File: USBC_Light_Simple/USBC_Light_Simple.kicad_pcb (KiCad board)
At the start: 2 copper layers, 79.5 x 40 mm, 11 parts, among them IC1 AP33772SDKZ-13-FA01, J1 USB_C_Receptacle, U1 XHP50B-00-0000-0D0BJ440E, U2 AL8861MP-13, U3 XHP50B-00-0000-0D0BJ440E, U4 XHP50B-00-0000-0D0BJ440E, U5 STM32C011F6Px, U6 AL8861MP-13, U7 XHP50B-00-0000-0D0BJ440E, U8 XHP50B-00-0000-0D0BJ440E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

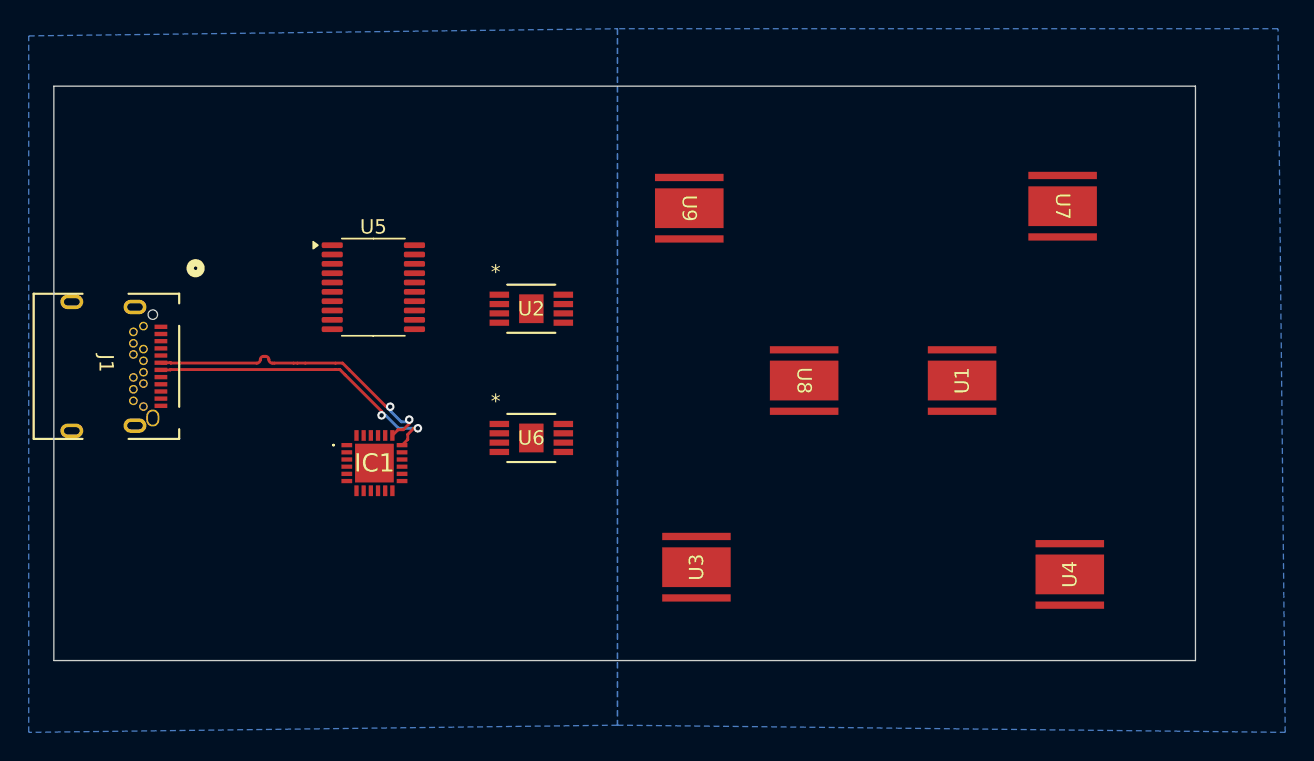
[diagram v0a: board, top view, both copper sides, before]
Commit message: Preliminary component placement on board.
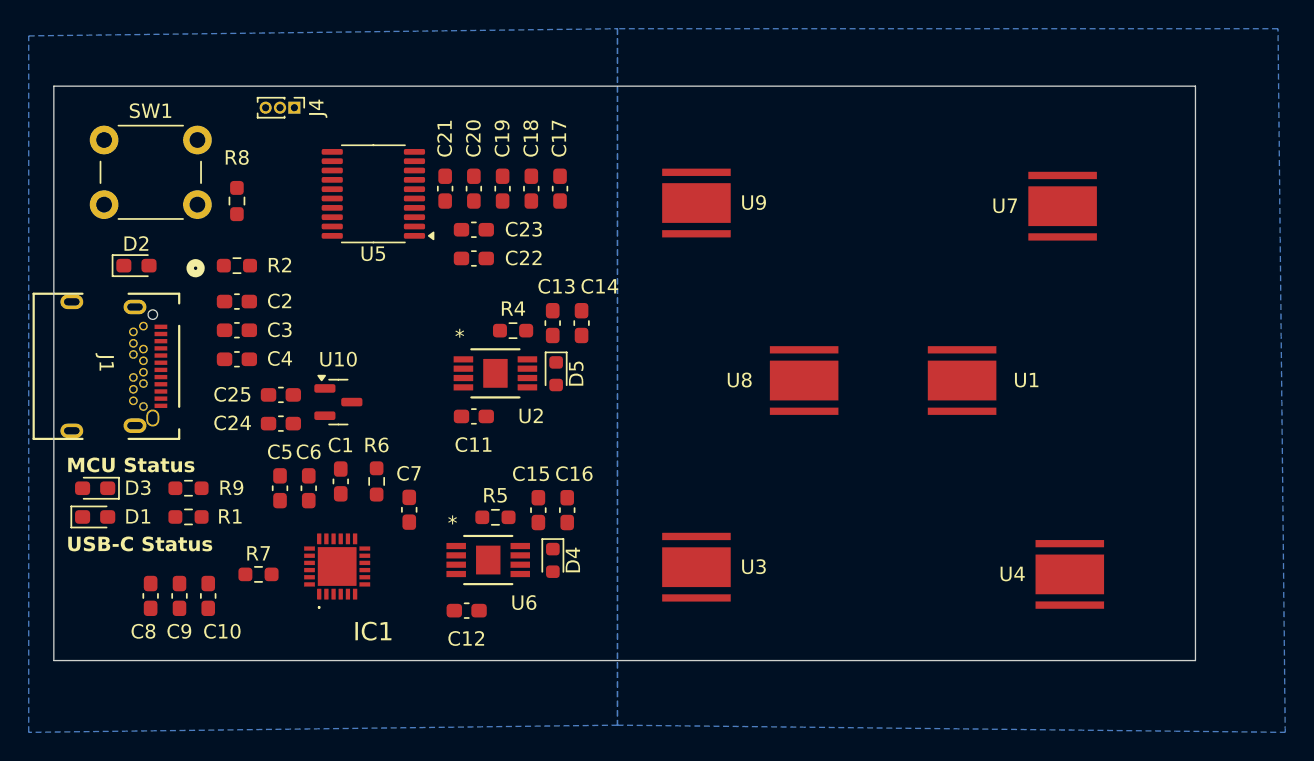
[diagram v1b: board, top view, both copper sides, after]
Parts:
- added C1: 100n, Capacitor_SMD:C_0603_1608Metric_Pad1.08x0.95mm_HandSolder, F.Cu at (113.7, 88.0)
- added C10: 100n, Capacitor_SMD:C_0603_1608Metric_Pad1.08x0.95mm_HandSolder, F.Cu at (104.5, 96.0)
- added C11: 100n, Capacitor_SMD:C_0603_1608Metric_Pad1.08x0.95mm_HandSolder, F.Cu at (123.0, 83.5)
- added C12: 100n, Capacitor_SMD:C_0603_1608Metric_Pad1.08x0.95mm_HandSolder, F.Cu at (122.5, 97.0)
- added C13: 100n, Capacitor_SMD:C_0603_1608Metric_Pad1.08x0.95mm_HandSolder, F.Cu at (128.5, 77.0)
- added C14: 1u, Capacitor_SMD:C_0603_1608Metric_Pad1.08x0.95mm_HandSolder, F.Cu at (130.5, 77.0)
- added C15: 100n, Capacitor_SMD:C_0603_1608Metric_Pad1.08x0.95mm_HandSolder, F.Cu at (127.5, 90.0)
- added C16: 1u, Capacitor_SMD:C_0603_1608Metric_Pad1.08x0.95mm_HandSolder, F.Cu at (129.5, 90.0)
- added C17: 1u, Capacitor_SMD:C_0603_1608Metric_Pad1.08x0.95mm_HandSolder, F.Cu at (129.0, 67.6)
- added C18: 1u, Capacitor_SMD:C_0603_1608Metric_Pad1.08x0.95mm_HandSolder, F.Cu at (127.0, 67.6)
- added C19: 100n, Capacitor_SMD:C_0603_1608Metric_Pad1.08x0.95mm_HandSolder, F.Cu at (125.0, 67.6)
- added C2: 10u, Capacitor_SMD:C_0603_1608Metric_Pad1.08x0.95mm_HandSolder, F.Cu at (106.5, 75.5)
- added C20: 100n, Capacitor_SMD:C_0603_1608Metric_Pad1.08x0.95mm_HandSolder, F.Cu at (123.0, 67.6)
- added C21: 10n, Capacitor_SMD:C_0603_1608Metric_Pad1.08x0.95mm_HandSolder, F.Cu at (121.0, 67.6)
- added C22: *, Capacitor_SMD:C_0603_1608Metric_Pad1.08x0.95mm_HandSolder, F.Cu at (123.0, 72.5)
- added C23: *, Capacitor_SMD:C_0603_1608Metric_Pad1.08x0.95mm_HandSolder, F.Cu at (123.0, 70.5)
- added C24: 1u, Capacitor_SMD:C_0603_1608Metric_Pad1.08x0.95mm_HandSolder, F.Cu at (109.6, 84.0)
- added C25: 100n, Capacitor_SMD:C_0603_1608Metric_Pad1.08x0.95mm_HandSolder, F.Cu at (109.6, 82.0)
- added C3: 1u, Capacitor_SMD:C_0603_1608Metric_Pad1.08x0.95mm_HandSolder, F.Cu at (106.5, 77.5)
- added C4: 100n, Capacitor_SMD:C_0603_1608Metric_Pad1.08x0.95mm_HandSolder, F.Cu at (106.5, 79.5)
- added C5: 1u, Capacitor_SMD:C_0603_1608Metric_Pad1.08x0.95mm_HandSolder, F.Cu at (109.5, 88.5)
- added C6: 100n, Capacitor_SMD:C_0603_1608Metric_Pad1.08x0.95mm_HandSolder, F.Cu at (111.5, 88.5)
- added C7: 100n, Capacitor_SMD:C_0603_1608Metric_Pad1.08x0.95mm_HandSolder, F.Cu at (118.5, 90.0)
- added C8: 10u, Capacitor_SMD:C_0603_1608Metric_Pad1.08x0.95mm_HandSolder, F.Cu at (100.5, 96.0)
- added C9: 1u, Capacitor_SMD:C_0603_1608Metric_Pad1.08x0.95mm_HandSolder, F.Cu at (102.5, 96.0)
- added D1: LED, LED_SMD:LED_0603_1608Metric_Pad1.05x0.95mm_HandSolder, F.Cu at (96.6, 90.5)
- added D2: LED, LED_SMD:LED_0603_1608Metric_Pad1.05x0.95mm_HandSolder, F.Cu at (99.5, 73.0)
- added D3: LED, LED_SMD:LED_0603_1608Metric_Pad1.05x0.95mm_HandSolder, F.Cu at (96.6, 88.5)
- added D4: D, Diode_SMD:D_0603_1608Metric, F.Cu at (128.5, 93.5)
- added D5: D, Diode_SMD:D_0603_1608Metric, F.Cu at (128.7, 80.5)
- added J4: Screw_Terminal_01x03, Connector_PinHeader_1.00mm:PinHeader_1x03_P1.00mm_Vertical, F.Cu at (110.5, 62.0)
- added R1: 1k, Resistor_SMD:R_0603_1608Metric_Pad0.98x0.95mm_HandSolder, F.Cu at (103.1, 90.5)
- added R2: 100k, Resistor_SMD:R_0603_1608Metric_Pad0.98x0.95mm_HandSolder, F.Cu at (106.5, 73.0)
- added R4: RS, Resistor_SMD:R_0603_1608Metric_Pad0.98x0.95mm_HandSolder, F.Cu at (125.7, 77.5)
- added R5: RS, Resistor_SMD:R_0603_1608Metric_Pad0.98x0.95mm_HandSolder, F.Cu at (124.5, 90.5)
- added R6: 10k, Resistor_SMD:R_0603_1608Metric_Pad0.98x0.95mm_HandSolder, F.Cu at (116.2, 88.0)
- added R7: 100, Resistor_SMD:R_0603_1608Metric_Pad0.98x0.95mm_HandSolder, F.Cu at (108.0, 94.5)
- added R8: 10k, Resistor_SMD:R_0603_1608Metric_Pad0.98x0.95mm_HandSolder, F.Cu at (106.5, 68.5)
- added R9: 1k, Resistor_SMD:R_0603_1608Metric_Pad0.98x0.95mm_HandSolder, F.Cu at (103.1, 88.5)
- added SW1: SW_Push, Button_Switch_THT:SW_PUSH_6mm, F.Cu at (97.2, 64.2)
- added U10: AP2127N-3.3, Package_TO_SOT_SMD:SOT-23, F.Cu at (113.6, 82.5)
- moved U6 9.01 mm to (124.0, 93.5)
- moved IC1 7.65 mm to (113.5, 94.0), turned to 90 degrees
- moved U5 6.50 mm to (116.0, 68.0), turned to 180 degrees
- moved U2 5.15 mm to (124.5, 80.5)
- moved U9 0.62 mm to (138.5, 68.6)
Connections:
- net /LEDs/LED_Input_Voltage renamed VLED
- net Net-(U2-LX-Pad5) renamed /LEDs/LX_1
- net Net-(U6-LX-Pad5) renamed /LEDs/LX_2
- IC1 pad 4: /USB_C_IC/USB_IC_SDA -> /MCU/I2C_SDA
- IC1 pad 5: /USB_C_IC/USB_IC_SCL -> /MCU/I2C_SCL
- U1 pad 1: unconnected-(U1-Pad1) -> /LEDs/LED_2
- U1 pad 3: unconnected-(U1-Pad3) -> Net-(U1-Pad3)
- U2 pad 1: unconnected-(U2-ISENSE-Pad1) -> /LEDs/LED_1
- U2 pad 4: Net-(U2-VSET) -> /LEDs/VSET_1
- U3 pad 1: unconnected-(U3-Pad1) -> Net-(U1-Pad3)
- U3 pad 3: unconnected-(U3-Pad3) -> Net-(U3-Pad3)
- U4 pad 1: unconnected-(U4-Pad1) -> Net-(U3-Pad3)
- U4 pad 3: unconnected-(U4-Pad3) -> Net-(L2-Pad1)
- U5 pad 1: unconnected-(U5-PB7-Pad1) -> /MCU/I2C_SDA
- U5 pad 11: unconnected-(U5-PA4-Pad11) -> /MCU/STATUS_LED
- U5 pad 18: unconnected-(U5-PA13-Pad18) -> /MCU/SWDIO
- U5 pad 19: unconnected-(U5-PA14-Pad19) -> /MCU/SWCLK
- U5 pad 2: unconnected-(U5-PC14-Pad2) -> /MCU/OSC_IN
- U5 pad 20: unconnected-(U5-PB6-Pad20) -> /MCU/I2C_SCL
- U5 pad 3: unconnected-(U5-PC15-Pad3) -> /MCU/OSC_OUT
- U5 pad 4: unconnected-(U5-VDD-Pad4) -> +3V3
- U5 pad 5: unconnected-(U5-VSS-Pad5) -> GND
- U5 pad 6: unconnected-(U5-PF2-Pad6) -> /MCU/NRST
- U5 pad 7: unconnected-(U5-PA0-Pad7) -> /MCU/UART_TX
- U5 pad 8: unconnected-(U5-PA1-Pad8) -> /MCU/UART_RX
- U6 pad 1: unconnected-(U6-ISENSE-Pad1) -> /LEDs/LED_2
- U6 pad 4: Net-(U6-VSET) -> /LEDs/VSET_2
- U7 pad 1: unconnected-(U7-Pad1) -> Net-(U7-Pad1)
- U7 pad 3: unconnected-(U7-Pad3) -> Net-(L1-Pad1)
- U8 pad 1: unconnected-(U8-Pad1) -> Net-(U8-Pad1)
- U8 pad 3: unconnected-(U8-Pad3) -> Net-(U7-Pad1)
- U9 pad 1: unconnected-(U9-Pad1) -> /LEDs/LED_1
- U9 pad 3: unconnected-(U9-Pad3) -> Net-(U8-Pad1)
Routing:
- net /USB_C_IC/data_-: track 21.6 -> 0.00 mm, vias 2 -> 0
- net /USB_C_IC/data_+: track 21.5 -> 0.00 mm, vias 2 -> 0
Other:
- board text added: "MCU Status"
- board text added: "USB-C Status"
